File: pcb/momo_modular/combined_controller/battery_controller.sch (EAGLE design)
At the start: 43 parts, among them Q1 P-MOSFET, Q2 P-MOSFET, U1 XRP7659, U2 MAX9938, U3 MCP1702, U4 PIC24F16KA101-X_PSSOP, U5 FLASH8MSOP8, U6 MCP73811

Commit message: Remove unnecessary transistor and current sense
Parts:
- removed C10: 100 nF, rcl:C-USC0402
- removed Q1: P-MOSFET, components:P-MOSFET
- removed R12: 100K, rcl:R-US_R0603
- removed R14: (no value), rcl:R-US_R0603
- removed U2: MAX9938, components:MAX9938
- JP1: DIGIKEY-PN 609-3263-ND -> S1011EC-06-ND
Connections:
- removed net CHG_CURR: C10.1, U2.OUT, U4.PGD2/AN1/VREF-/CN3/RA1
- removed net N$3: Q1.DRAIN, R7.2
- removed net N$4: C8.1, R14.1, U2.RS+, U6.VBAT
- removed net SAMP_EN: Q1.GATE, R12.2, U4.U1RX/U1BCLK/CN6/RB2
- net GND: no longer C10.2, U2.GND
- net V+: now also C8.1, R7.2, U6.VBAT; no longer Q1.SOURCE, R12.1, R14.2, U2.RS-
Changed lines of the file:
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@@
 <attribute name="DIGIKEY-PN" value="A19450-ND"/>
-</part>
-<part name="Q1" library="components" deviceset="P-MOSFET" device=""/>
-<part name="R12" library="rcl" deviceset="R-US_" device="R0603" value="100K">
-<attribute name="DIGIKEY-PN" value="P100KHCT-ND"/>
 </part>
 <part name="VCC2" library="supply1" deviceset="VCCIO" device=""/>
@@
 <part name="VCC10" library="supply1" deviceset="VCCINT" device=""/>
 <part name="GND5" library="supply1" deviceset="GND" device=""/>
-<part name="P+3" library="supply1" deviceset="V+" device="">
-<attribute name="DIGIKEY-PN" value="PIC24F16KA101-I/SS-ND"/>
-</part>
 <part name="R5" library="rcl" deviceset="R-US_" device="R0603" value="10K">
 <attribute name="DIGIKEY-PN" value="P10.0KHCT-ND"/>
@@
 <part name="JP2" library="components" deviceset="MOMO-EDGE-6F" device=""/>
 <part name="JP1" library="components" deviceset="MOMO-VERT-6M" device="">
-<attribute name="DIGIKEY-PN" value="609-3263-ND"/>
+<attribute name="DIGIKEY-PN" value="S1011EC-06-ND"/>
 </part>
 <part name="JP3" library="pinhead" deviceset="PINHD-1X1" device=""/>
@@
 <attribute name="DIGIKEY-PN" value="SL13HE3/61TGICT-ND"/>
 </part>
-<part name="U2" library="components" deviceset="MAX9938" device="">
-<attribute name="DIGIKEY-PN" value=""/>
-<attribute name="DIGIKEY-PN-BATT" value="MAX9938FEUK+TCT-ND"/>
-<attribute name="DIGIKEY-PN-SOLAR" value="MAX9938FEUK+TCT-ND"/>
-</part>
 <part name="U6" library="components" deviceset="MCP73811" device="">
 <attribute name="DIGIKEY-PN" value=""/>
 <attribute name="DIGIKEY-PN-BATT" value="MCP73811T-420I/OTCT-ND"/>
 <attribute name="DIGIKEY-PN-SOLAR" value="MCP73811T-420I/OTCT-ND"/>
-</part>
-<part name="R14" library="rcl" deviceset="R-US_" device="R0603">
-<attribute name="DIGIKEY-PN-BATT" value="P.12AJCT-ND"/>
-<attribute name="DIGIKEY-PN-SOLAR" value="P.12AJCT-ND"/>
-</part>
-<part name="C10" library="rcl" deviceset="C-US" device="C0402" value="100 nF">
-<attribute name="DIGIKEY-PN-BATT" value="587-2985-1-ND"/>
-<attribute name="DIGIKEY-PN-SOLAR" value="587-2985-1-ND"/>
 </part>
 </parts>
@@
 <instance part="GND7" gate="1" x="-33.02" y="-104.14"/>
 <instance part="GND12" gate="1" x="-208.28" y="91.44"/>
-<instance part="P+10" gate="1" x="-116.84" y="-58.42"/>
+<instance part="P+10" gate="1" x="-116.84" y="-68.58"/>
 <instance part="C6" gate="G$1" x="-127" y="91.44">
 <attribute name="DIGIKEY-PN-BATT" x="-127" y="91.44" size="1.778" layer="96" display="off"/>
@@
 <instance part="JP4" gate="G$1" x="-30.48" y="-76.2">
 <attribute name="DIGIKEY-PN" x="-30.48" y="-76.2" size="1.778" layer="96" display="off"/>
-</instance>
-<instance part="Q1" gate="G$1" x="-116.84" y="-66.04"/>
-<instance part="R12" gate="G$1" x="-129.54" y="-58.42" rot="R270">
-<attribute name="DIGIKEY-PN" x="-129.54" y="-58.42" size="1.778" layer="96" rot="R270" display="off"/>
 </instance>
 <instance part="VCC2" gate="G$1" x="-30.48" y="15.24"/>
@@
 <instance part="VCC10" gate="G$1" x="-88.9" y="-83.82"/>
 <instance part="GND5" gate="1" x="-78.74" y="2.54"/>
-<instance part="P+3" gate="1" x="-129.54" y="-50.8">
-<attribute name="DIGIKEY-PN" x="-129.54" y="-50.8" size="1.778" layer="96" display="off"/>
-</instance>
 <instance part="R5" gate="G$1" x="-215.9" y="22.86" rot="R90">
 <attribute name="DIGIKEY-PN" x="-215.9" y="22.86" size="1.778" layer="96" rot="R90" display="off"/>
@@
 <instance part="D2" gate="G$1" x="-215.9" y="104.14">
 <attribute name="DIGIKEY-PN" x="-215.9" y="104.14" size="1.778" layer="96" display="off"/>
-</instance>
-<instance part="U2" gate="G$1" x="-55.88" y="81.28">
-<attribute name="DIGIKEY-PN-BATT" x="-55.88" y="81.28" size="1.778" layer="96" display="off"/>
-<attribute name="DIGIKEY-PN-SOLAR" x="-55.88" y="81.28" size="1.778" layer="96" display="off"/>
 </instance>
 <instance part="U6" gate="G$1" x="-106.68" y="93.98" smashed="yes">
@@
 <attribute name="DIGIKEY-PN-BATT" x="-106.68" y="93.98" size="1.778" layer="96" display="off"/>
 <attribute name="DIGIKEY-PN-SOLAR" x="-106.68" y="93.98" size="1.778" layer="96" display="off"/>
-</instance>
-<instance part="R14" gate="G$1" x="-58.42" y="101.6">
-<attribute name="DIGIKEY-PN-BATT" x="-58.42" y="101.6" size="1.778" layer="96" display="off"/>
-<attribute name="DIGIKEY-PN-SOLAR" x="-58.42" y="101.6" size="1.778" layer="96" display="off"/>
-</instance>
-<instance part="C10" gate="G$1" x="-45.72" y="81.28">
-<attribute name="DIGIKEY-PN-BATT" x="-45.72" y="81.28" size="1.778" layer="96" display="off"/>
-<attribute name="DIGIKEY-PN-SOLAR" x="-45.72" y="81.28" size="1.778" layer="96" display="off"/>
 </instance>
 </instances>
@@
 <wire x1="-96.52" y1="76.2" x2="-116.84" y2="76.2" width="0.1524" layer="91"/>
 <wire x1="-116.84" y1="76.2" x2="-127" y2="76.2" width="0.1524" layer="91"/>
-<wire x1="-17.78" y1="76.2" x2="-45.72" y2="76.2" width="0.1524" layer="91"/>
 <pinref part="C9" gate="G$1" pin="2"/>
-<wire x1="-45.72" y1="76.2" x2="-60.96" y2="76.2" width="0.1524" layer="91"/>
-<wire x1="-60.96" y1="76.2" x2="-78.74" y2="76.2" width="0.1524" layer="91"/>
+<wire x1="-17.78" y1="76.2" x2="-78.74" y2="76.2" width="0.1524" layer="91"/>
 <wire x1="0" y1="86.36" x2="0" y2="76.2" width="0.1524" layer="91"/>
 <wire x1="0" y1="76.2" x2="-17.78" y2="76.2" width="0.1524" layer="91"/>
@@
 <wire x1="-78.74" y1="91.44" x2="-78.74" y2="76.2" width="0.1524" layer="91"/>
 <junction x="-78.74" y="76.2"/>
-<pinref part="U2" gate="G$1" pin="GND"/>
-<junction x="-60.96" y="76.2"/>
 <pinref part="U6" gate="G$1" pin="GND"/>
 <wire x1="-96.52" y1="83.82" x2="-96.52" y2="76.2" width="0.1524" layer="91"/>
 <junction x="-96.52" y="76.2"/>
-<pinref part="C10" gate="G$1" pin="2"/>
-<junction x="-45.72" y="76.2"/>
 </segment>
 <segment>
@@
 <pinref part="U3" gate="G$1" pin="VIN"/>
 <wire x1="-30.48" y1="101.6" x2="-35.56" y2="101.6" width="0.1524" layer="91"/>
-<pinref part="R14" gate="G$1" pin="2"/>
-<pinref part="U2" gate="G$1" pin="RS-"/>
-<wire x1="-53.34" y1="101.6" x2="-53.34" y2="99.06" width="0.1524" layer="91"/>
 <wire x1="-35.56" y1="101.6" x2="-43.18" y2="101.6" width="0.1524" layer="91"/>
 <junction x="-35.56" y="101.6"/>
-<junction x="-53.34" y="101.6"/>
 <pinref part="R4" gate="G$1" pin="2"/>
-<wire x1="-43.18" y1="101.6" x2="-53.34" y2="101.6" width="0.1524" layer="91"/>
 <wire x1="-73.66" y1="114.3" x2="-43.18" y2="114.3" width="0.1524" layer="91"/>
 <wire x1="-43.18" y1="114.3" x2="-43.18" y2="101.6" width="0.1524" layer="91"/>
 <junction x="-43.18" y="101.6"/>
-</segment>
-<segment>
-<pinref part="Q1" gate="G$1" pin="SOURCE"/>
-<pinref part="P+10" gate="1" pin="V+"/>
+<pinref part="C8" gate="G$1" pin="1"/>
+<wire x1="-78.74" y1="99.06" x2="-78.74" y2="101.6" width="0.1524" layer="91"/>
+<wire x1="-78.74" y1="101.6" x2="-43.18" y2="101.6" width="0.1524" layer="91"/>
+<pinref part="U6" gate="G$1" pin="VBAT"/>
+<wire x1="-86.36" y1="101.6" x2="-78.74" y2="101.6" width="0.1524" layer="91"/>
+<junction x="-78.74" y="101.6"/>
 </segment>
 <segment>
@@
 </segment>
 <segment>
-<pinref part="R12" gate="G$1" pin="1"/>
-<pinref part="P+3" gate="1" pin="V+"/>
-</segment>
-<segment>
 <pinref part="P+2" gate="1" pin="V+"/>
 <pinref part="JP2" gate="G$1" pin="4V"/>
@@
 <pinref part="P+1" gate="1" pin="V+"/>
 <pinref part="JP1" gate="G$1" pin="4V"/>
+</segment>
+<segment>
+<pinref part="R7" gate="G$1" pin="2"/>
+<pinref part="P+10" gate="1" pin="V+"/>
 </segment>
 </net>
@@
 </segment>
 </net>
-<net name="N$3" class="0">
-<segment>
-<pinref part="R7" gate="G$1" pin="2"/>
-<pinref part="Q1" gate="G$1" pin="DRAIN"/>
-</segment>
-</net>
-<net name="SAMP_EN" class="0">
-<segment>
-<pinref part="R12" gate="G$1" pin="2"/>
-<pinref part="Q1" gate="G$1" pin="GATE"/>
-<wire x1="-129.54" y1="-63.5" x2="-121.92" y2="-63.5" width="0.1524" layer="91"/>
-<wire x1="-129.54" y1="-63.5" x2="-139.7" y2="-63.5" width="0.1524" layer="91"/>
-<junction x="-129.54" y="-63.5"/>
-<label x="-139.7" y="-63.5" size="1.778" layer="95"/>
-</segment>
-<segment>
-<pinref part="U4" gate="A" pin="U1RX/U1BCLK/CN6/RB2"/>
-<wire x1="-193.04" y1="-2.54" x2="-198.12" y2="-2.54" width="0.1524" layer="91"/>
-<label x="-200.66" y="-2.54" size="1.778" layer="95"/>
-</segment>
-</net>
 <net name="VCCIO" class="0">
 <segment>
@@
 </segment>
 </net>
-<net name="N$4" class="0">
-<segment>
-<pinref part="R14" gate="G$1" pin="1"/>
-<pinref part="U2" gate="G$1" pin="RS+"/>
-<wire x1="-63.5" y1="101.6" x2="-63.5" y2="99.06" width="0.1524" layer="91"/>
-<pinref part="C8" gate="G$1" pin="1"/>
-<wire x1="-78.74" y1="99.06" x2="-78.74" y2="101.6" width="0.1524" layer="91"/>
-<wire x1="-78.74" y1="101.6" x2="-63.5" y2="101.6" width="0.1524" layer="91"/>
-<junction x="-63.5" y="101.6"/>
-<pinref part="U6" gate="G$1" pin="VBAT"/>
-<wire x1="-86.36" y1="101.6" x2="-78.74" y2="101.6" width="0.1524" layer="91"/>
-<junction x="-78.74" y="101.6"/>
-</segment>
-</net>
-<net name="CHG_CURR" class="0">
-<segment>
-<pinref part="U4" gate="A" pin="PGD2/AN1/VREF-/CN3/RA1"/>
-<wire x1="-78.74" y1="-12.7" x2="-63.5" y2="-12.7" width="0.1524" layer="91"/>
-<label x="-78.74" y="-12.7" size="1.778" layer="95"/>
-</segment>
-<segment>
-<pinref part="U2" gate="G$1" pin="OUT"/>
-<pinref part="C10" gate="G$1" pin="1"/>
-<wire x1="-48.26" y1="83.82" x2="-45.72" y2="83.82" width="0.1524" layer="91"/>
-<wire x1="-45.72" y1="83.82" x2="-35.56" y2="83.82" width="0.1524" layer="91"/>
-<junction x="-45.72" y="83.82"/>
-<label x="-43.18" y="83.82" size="1.778" layer="95"/>
-</segment>
-</net>

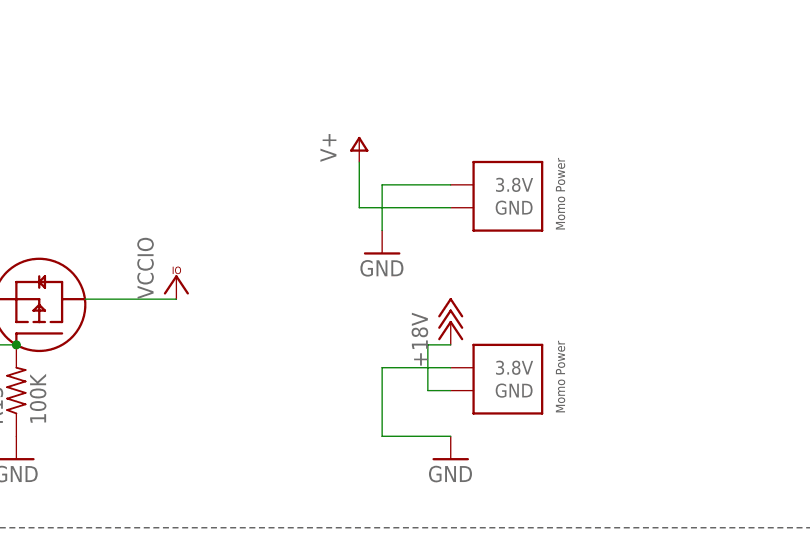
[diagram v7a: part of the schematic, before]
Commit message: Re-layout the controller board for 1M form factor
Not done but mostly there.
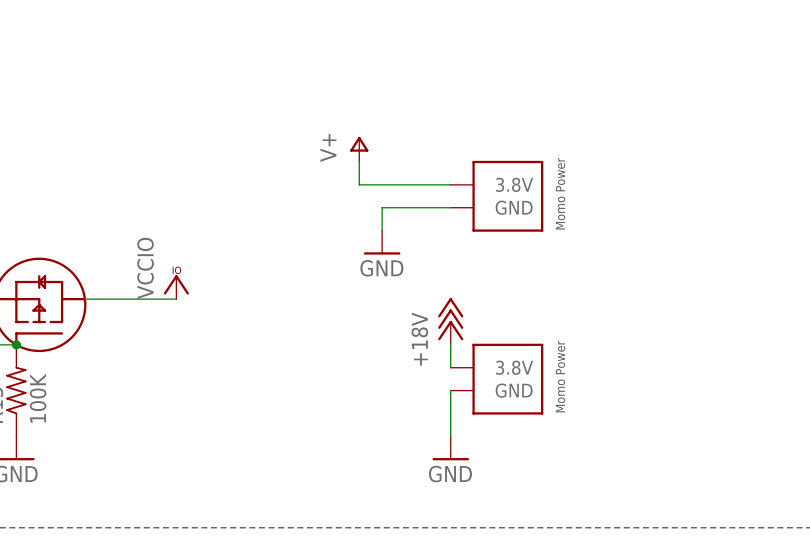
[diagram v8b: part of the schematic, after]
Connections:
- net +18V: now also JP5.3.8V; no longer JP5.GND
- net GND: now also JP4.GND, JP5.GND; no longer JP4.3.8V, JP5.3.8V
- net V+: now also JP4.3.8V; no longer JP4.GND
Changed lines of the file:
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@@
-</segment>
-<segment>
-<pinref part="GND8" gate="1" pin="GND"/>
-<wire x1="-40.64" y1="-78.74" x2="-40.64" y2="-73.66" width="0.1524" layer="91"/>
-<pinref part="JP4" gate="G$1" pin="3.8V"/>
-<wire x1="-40.64" y1="-73.66" x2="-33.02" y2="-73.66" width="0.1524" layer="91"/>
 </segment>
 <segment>
@@
 <segment>
 <pinref part="GND7" gate="1" pin="GND"/>
-<wire x1="-33.02" y1="-101.6" x2="-40.64" y2="-101.6" width="0.1524" layer="91"/>
-<wire x1="-40.64" y1="-101.6" x2="-40.64" y2="-93.98" width="0.1524" layer="91"/>
-<pinref part="JP5" gate="G$1" pin="3.8V"/>
-<wire x1="-40.64" y1="-93.98" x2="-33.02" y2="-93.98" width="0.1524" layer="91"/>
+<pinref part="JP5" gate="G$1" pin="GND"/>
+<wire x1="-33.02" y1="-101.6" x2="-33.02" y2="-96.52" width="0.1524" layer="91"/>
+</segment>
+<segment>
+<pinref part="JP4" gate="G$1" pin="GND"/>
+<pinref part="GND8" gate="1" pin="GND"/>
+<wire x1="-33.02" y1="-76.2" x2="-40.64" y2="-76.2" width="0.1524" layer="91"/>
+<wire x1="-40.64" y1="-76.2" x2="-40.64" y2="-78.74" width="0.1524" layer="91"/>
 </segment>
 </net>
@@
 </segment>
 <segment>
-<pinref part="JP4" gate="G$1" pin="GND"/>
-<pinref part="P+8" gate="1" pin="V+"/>
-<wire x1="-33.02" y1="-76.2" x2="-43.18" y2="-76.2" width="0.1524" layer="91"/>
-<wire x1="-43.18" y1="-76.2" x2="-43.18" y2="-71.12" width="0.1524" layer="91"/>
-</segment>
-<segment>
 <pinref part="P+2" gate="1" pin="V+"/>
 <pinref part="JP2" gate="G$1" pin="4V"/>
@@
 <pinref part="R7" gate="G$1" pin="2"/>
 <pinref part="P+10" gate="1" pin="V+"/>
+</segment>
+<segment>
+<pinref part="P+8" gate="1" pin="V+"/>
+<wire x1="-33.02" y1="-73.66" x2="-43.18" y2="-73.66" width="0.1524" layer="91"/>
+<wire x1="-43.18" y1="-73.66" x2="-43.18" y2="-71.12" width="0.1524" layer="91"/>
+<pinref part="JP4" gate="G$1" pin="3.8V"/>
 </segment>
 </net>
@@
 <net name="+18V" class="0">
 <segment>
-<pinref part="P+5" gate="1" pin="+18V"/>
-<wire x1="-33.02" y1="-91.44" x2="-35.56" y2="-91.44" width="0.1524" layer="91"/>
-<wire x1="-35.56" y1="-91.44" x2="-35.56" y2="-96.52" width="0.1524" layer="91"/>
-<pinref part="JP5" gate="G$1" pin="GND"/>
-<wire x1="-35.56" y1="-96.52" x2="-33.02" y2="-96.52" width="0.1524" layer="91"/>
-</segment>
-<segment>
 <pinref part="D2" gate="G$1" pin="A"/>
 <pinref part="P+6" gate="1" pin="+18V"/>
@@
 <wire x1="-220.98" y1="104.14" x2="-220.98" y2="109.22" width="0.1524" layer="91"/>
 </segment>
-</net>
+<segment>
+<pinref part="JP5" gate="G$1" pin="3.8V"/>
+<pinref part="P+5" gate="1" pin="+18V"/>
+<wire x1="-33.02" y1="-93.98" x2="-33.02" y2="-91.44" width="0.1524" layer="91"/>
+</segment>
+</net>
